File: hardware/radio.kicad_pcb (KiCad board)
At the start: 2 copper layers, 100 x 50 mm, 61 parts, among them J1 105450-0101, J2 Conn_01x02, J3 Conn_01x02, J4 Conn_01x04, J5 Conn_01x02_Male, Q1 Q_PMOS_DGS, Q2 Q_NMOS_DGS, Q3 Q_NMOS_DGS, Q4 Q_PMOS_DGS, SW1 SW_BOOT, SW2 SW_RST, SW3 SW_1, SW4 Rot_Enc, SW5 SW_2, SW6 SW_3, U1 TP4056, U2 ESP32-WROOM-32, U3 TPS5432, U4 MAX98357

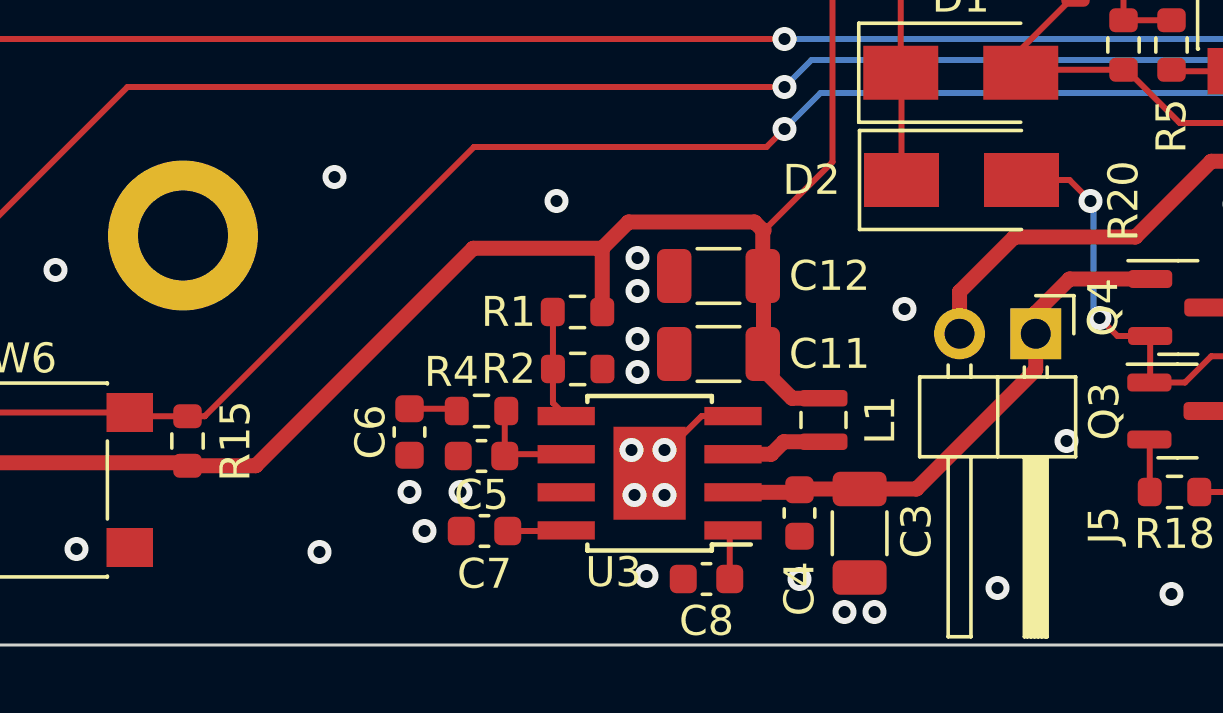
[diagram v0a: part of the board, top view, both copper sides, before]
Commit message: Fixed C8 connection from BOOT-GND to BOOT-PH
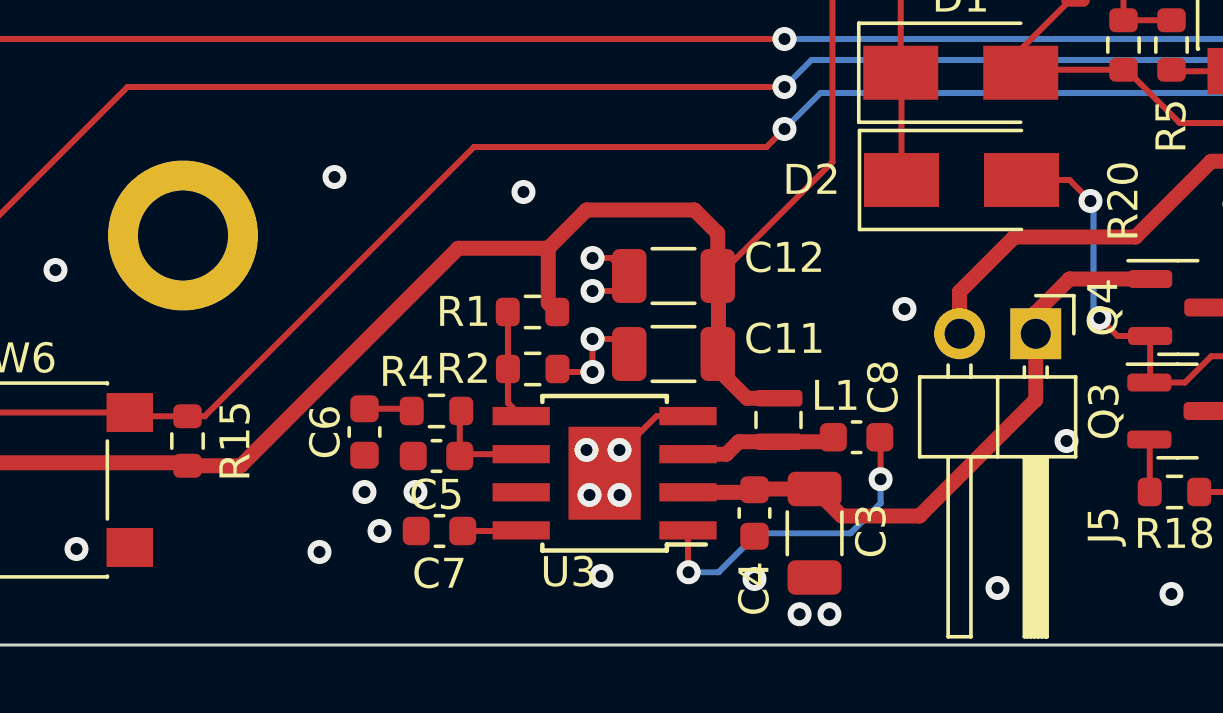
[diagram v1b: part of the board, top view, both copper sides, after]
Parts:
- moved C8 6.88 mm to (94.1, 73.1)
- moved C11 1.50 mm to (88.0, 70.3)
- moved C12 1.50 mm to (88.0, 67.7)
- moved C3 1.50 mm to (92.7, 76.3)
- moved C4 1.50 mm to (90.7, 75.6)
- moved C5 1.50 mm to (80.1, 73.7)
- moved C6 1.50 mm to (77.7, 72.9)
- moved C7 1.50 mm to (80.2, 76.2)
- moved L1 1.50 mm to (91.5, 72.5)
- moved R1 1.50 mm to (83.3, 68.9)
- moved R2 1.50 mm to (83.3, 70.8)
- moved R4 1.50 mm to (80.1, 72.2)
- moved U3 1.50 mm to (85.7, 74.3)
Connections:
- C8 pad 1: GND -> Net-(C8-Pad1)
- L1 pad 1: Net-(L1-Pad1) -> Net-(C8-Pad1)
- U3 pad 3: Net-(L1-Pad1) -> Net-(C8-Pad1)
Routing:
- net Net-(C8-Pad2): track 1.66 -> 11.0 mm, vias 0 -> 2
- net GND: track 55.6 -> 62.2 mm
- net Net-(C8-Pad1): track 0.00 -> 5.08 mm
- net Net-(L1-Pad1): track 3.19 -> 0.00 mm
- net Net-(C3-Pad1): track 18.0 -> 20.8 mm
- net +3V3: track 256.3 -> 257.3 mm

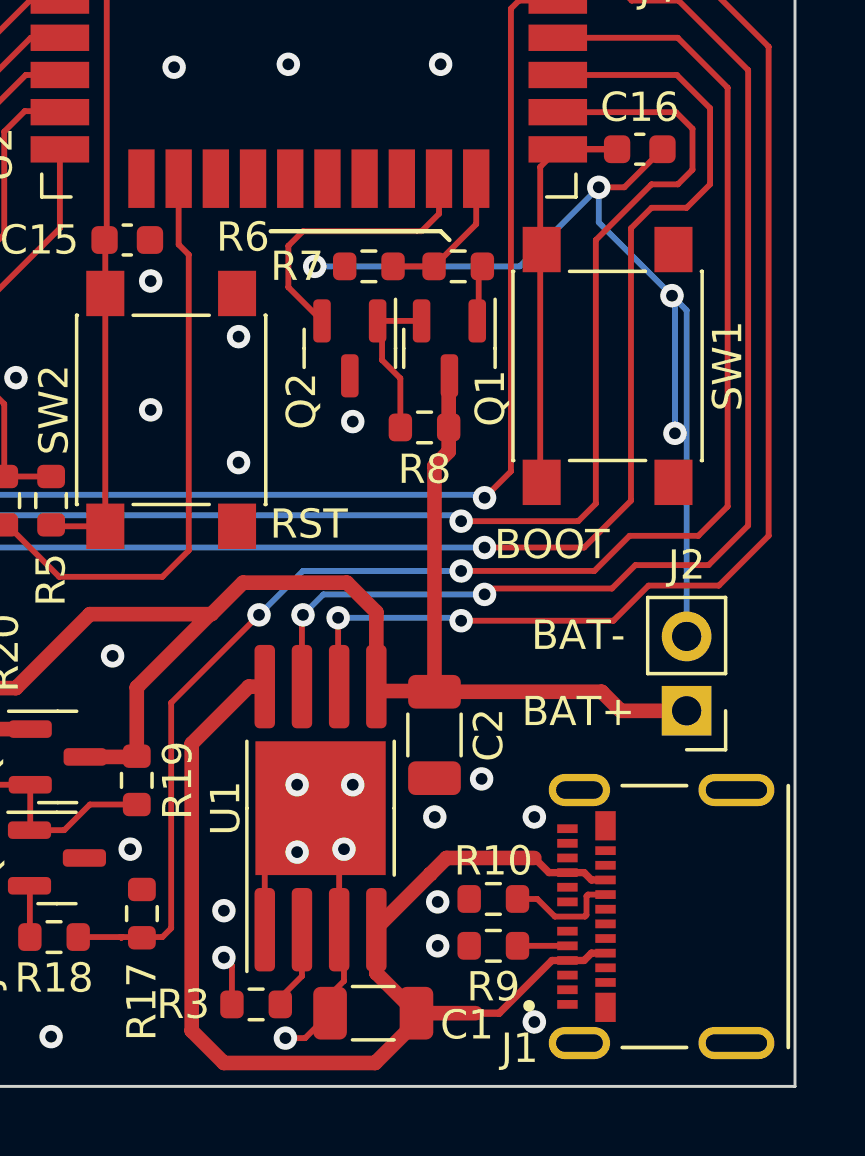
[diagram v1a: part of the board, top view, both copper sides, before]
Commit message: Added 0.4 ohm 0.5 W resistor to TP4056 to help with power dissipation
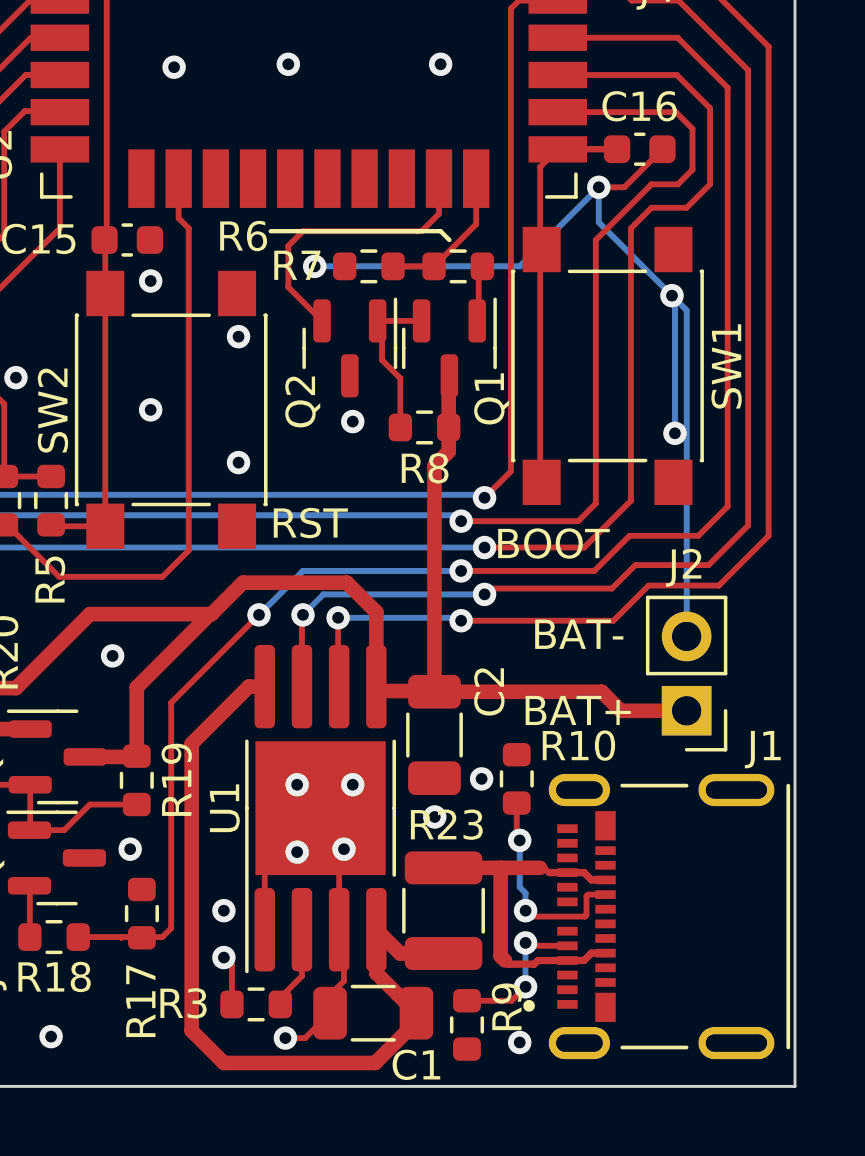
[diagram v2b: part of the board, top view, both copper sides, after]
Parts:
- added R23: 0.4, Resistor_SMD:R_1210_3225Metric, F.Cu at (118.0, 74.0)
- moved R10 4.18 mm to (120.5, 69.5), turned to 90 degrees
- moved R9 2.85 mm to (118.8, 77.9), turned to -90 degrees
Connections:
- C1 pad 1: +5V -> Net-(C1-Pad1)
- U1 pad 4: +5V -> Net-(C1-Pad1)
- U1 pad 8: +5V -> Net-(C1-Pad1)
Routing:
- net +5V: track 42.4 -> 13.0 mm
- net Net-(C1-Pad1): track 0.00 -> 28.2 mm
- net Net-(J1-PadA5): track 1.61 -> 5.17 mm, vias 0 -> 2
- net Net-(J1-PadB5): track 4.14 -> 7.50 mm, vias 0 -> 2
- net GND: vias 100 -> 97

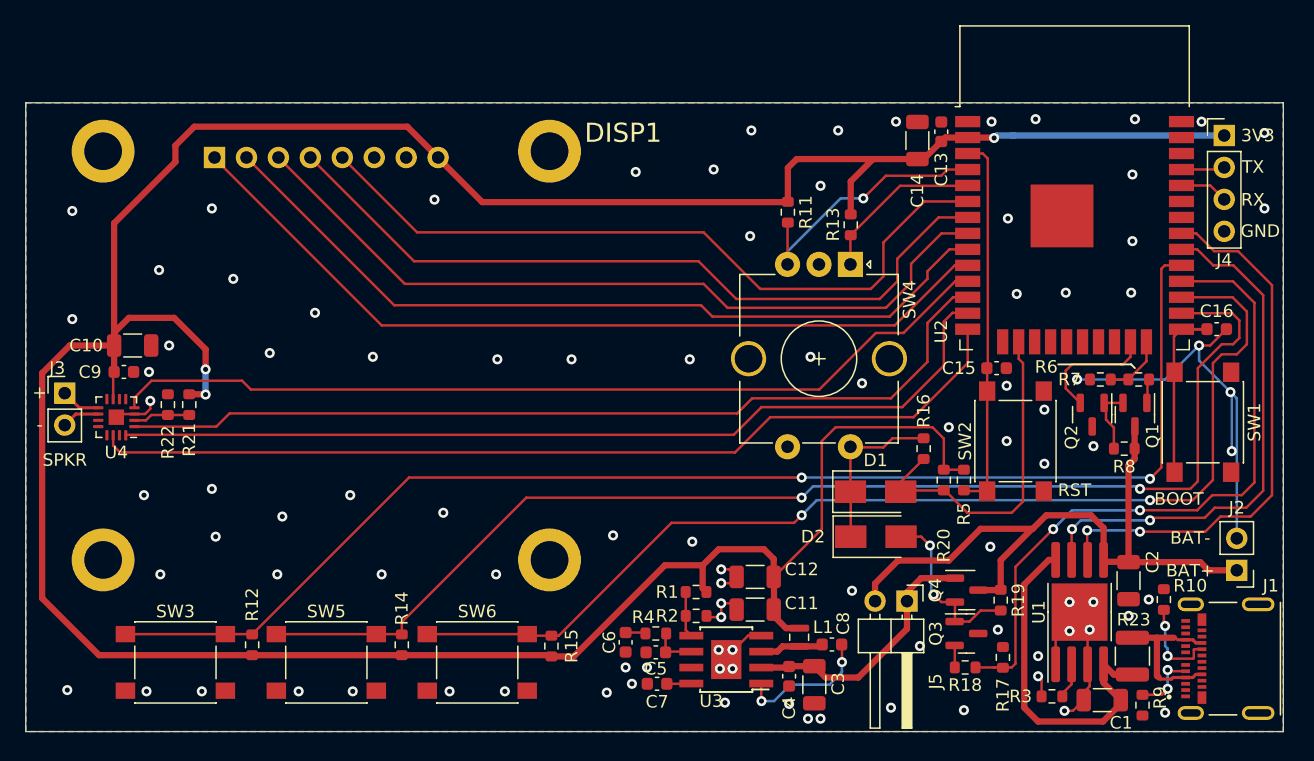
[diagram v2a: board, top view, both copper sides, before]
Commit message: adjusted silkscreen and some vias to improve labeling consistency and readability
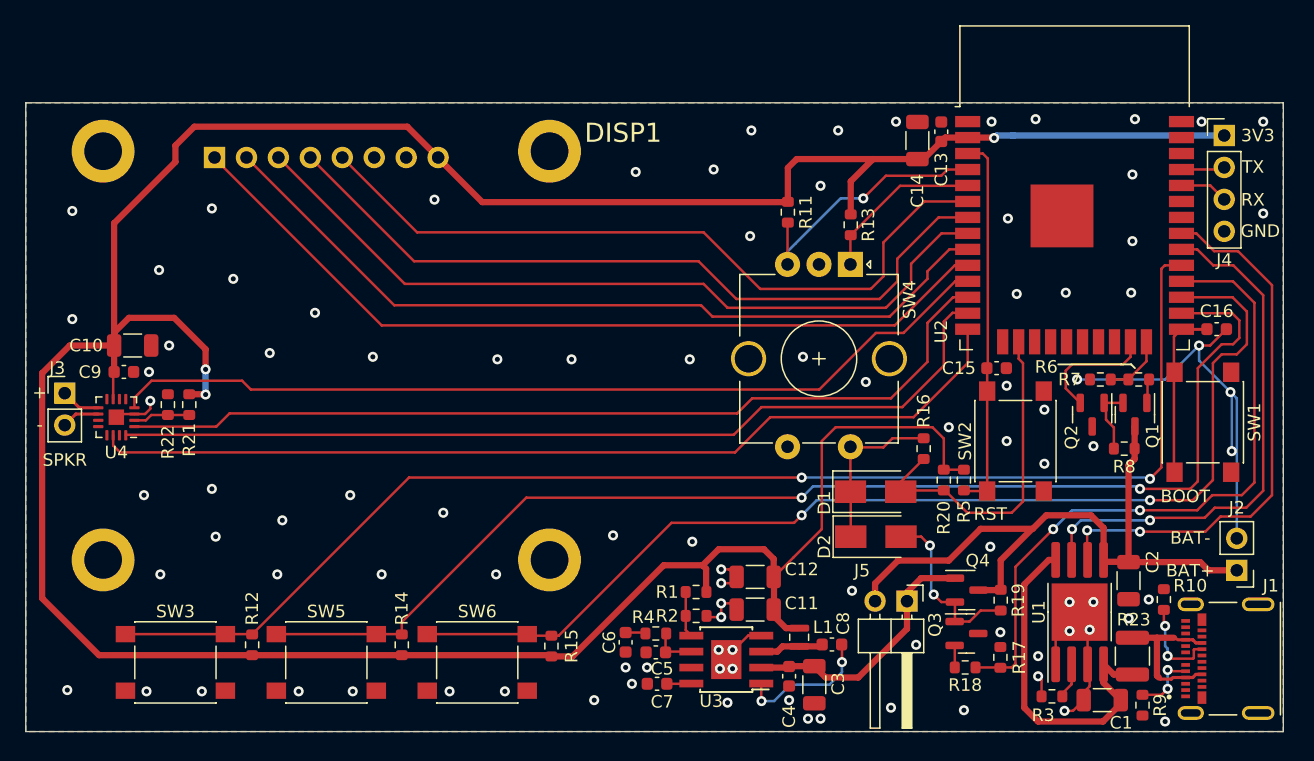
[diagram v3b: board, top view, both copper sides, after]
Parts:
- moved R17 0.20 mm to (107.5, 74.1)

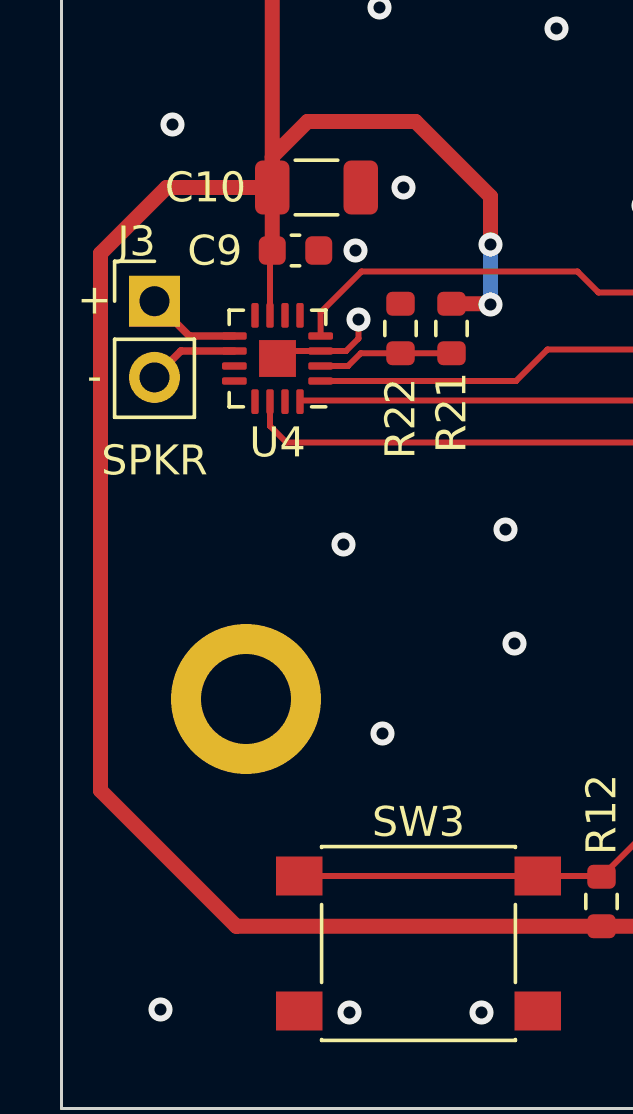
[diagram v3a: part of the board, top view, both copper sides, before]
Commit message: added copper fill cutout to the speaker connector and adjusted the 3V3 power trace near it to reduce potential proximity/ground-plane induced crosstalk
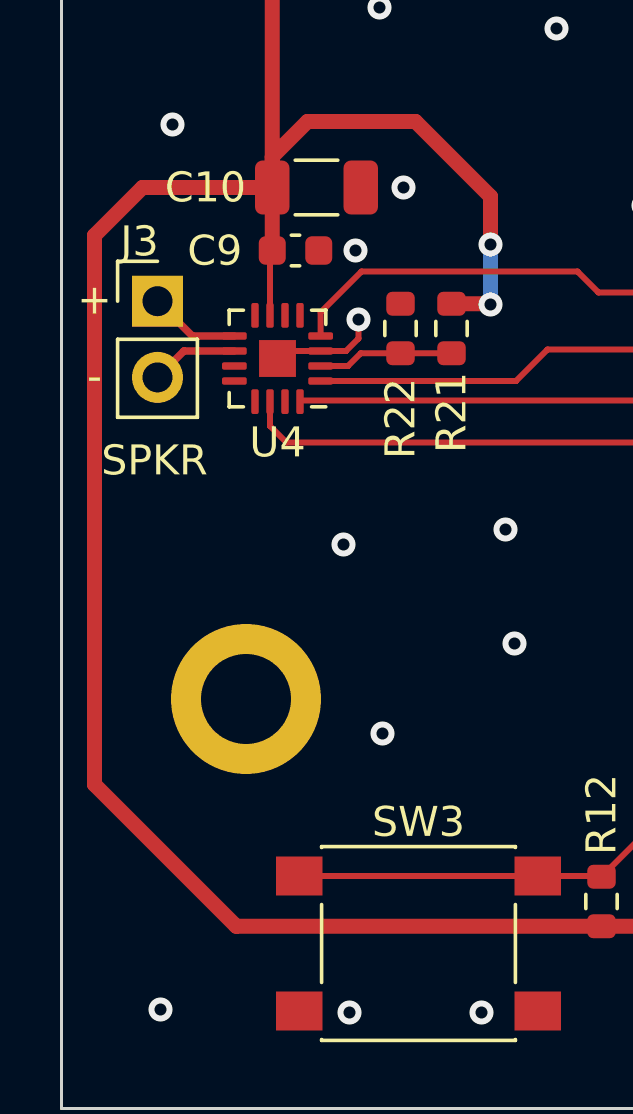
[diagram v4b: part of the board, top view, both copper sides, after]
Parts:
- moved J3 0.10 mm to (33.2, 53.1)
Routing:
- net +3V3: track 257.3 -> 257.9 mm
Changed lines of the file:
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@@
   )
   (footprint "Connector_PinHeader_2.54mm:PinHeader_1x02_P2.54mm_Vertical" (layer "F.Cu")
-    (at 33.1 53.09)
+    (at 33.2 53.09)
     (descr "Through hole straight pin header, 1x02, 2.54mm pitch, single row")
     (tags "Through hole pin header THT 1x02 2.54mm single row")
@@
   (segment (start 89.5 67.725) (end 89.475 67.7) (width 0.5) (layer "F.Cu") (net 7))
   (segment (start 94.4 55.8) (end 102.1 55.8) (width 0.2) (layer "F.Cu") (net 7))
+  (segment (start 31.1 69.2) (end 31.1 50.9) (width 0.5) (layer "F.Cu") (net 7))
   (segment (start 90.575 37.9) (end 90.6 37.875) (width 0.5) (layer "F.Cu") (net 7))
   (segment (start 89.5 67.7) (end 91.025 66.175) (width 0.2) (layer "F.Cu") (net 7))
@@
   (segment (start 102.1 55.8) (end 103 56.7) (width 0.2) (layer "F.Cu") (net 7))
   (segment (start 73.475 74.025) (end 80.725 66.775) (width 0.5) (layer "F.Cu") (net 7))
-  (segment (start 31.3 51.5) (end 33.5 49.3) (width 0.5) (layer "F.Cu") (net 7))
+  (segment (start 32.7 49.3) (end 37.025 49.3) (width 0.5) (layer "F.Cu") (net 7))
   (segment (start 43.4 31.9) (end 60.34 31.9) (width 0.5) (layer "F.Cu") (net 7))
   (segment (start 48 73.925) (end 59.9 73.925) (width 0.5) (layer "F.Cu") (net 7))
   (segment (start 95.6 36.25) (end 97.375 34.475) (width 0.5) (layer "F.Cu") (net 7))
+  (segment (start 31.1 50.9) (end 32.7 49.3) (width 0.5) (layer "F.Cu") (net 7))
   (segment (start 71.7 73.925) (end 71.8 74.025) (width 0.5) (layer "F.Cu") (net 7))
   (segment (start 43 53.175) (end 44.275 53.175) (width 0.5) (layer "F.Cu") (net 7))
   (segment (start 95.6 38.875) (end 95.6 36.25) (width 0.5) (layer "F.Cu") (net 7))
   (segment (start 60.34 31.9) (end 62.79 34.35) (width 0.5) (layer "F.Cu") (net 7))
-  (segment (start 48 73.925) (end 35.825 73.925) (width 0.5) (layer "F.Cu") (net 7))
   (segment (start 36.95 51.475) (end 37.025 51.4) (width 0.5) (layer "F.Cu") (net 7))
   (segment (start 103 59.175) (end 104.6 59.175) (width 0.2) (layer "F.Cu") (net 7))
@@
   (segment (start 71.8 74.025) (end 73.475 74.025) (width 0.5) (layer "F.Cu") (net 7))
   (segment (start 89.5 70.825) (end 89.5 67.725) (width 0.5) (layer "F.Cu") (net 7))
-  (segment (start 33.5 49.3) (end 37.025 49.3) (width 0.5) (layer "F.Cu") (net 7))
+  (segment (start 35.825 73.925) (end 31.1 69.2) (width 0.5) (layer "F.Cu") (net 7))
   (segment (start 85.1 65.5) (end 88.7 65.5) (width 0.5) (layer "F.Cu") (net 7))
   (segment (start 80.725 66.775) (end 83.825 66.775) (width 0.5) (layer "F.Cu") (net 7))
@@
   (segment (start 93.3 63.9) (end 93.3 56.9) (width 0.2) (layer "F.Cu") (net 7))
   (segment (start 104.9 32.765) (end 106.965 32.765) (width 0.5) (layer "F.Cu") (net 7))
-  (segment (start 31.3 69.4) (end 31.3 51.5) (width 0.5) (layer "F.Cu") (net 7))
+  (segment (start 48 73.925) (end 35.825 73.925) (width 0.5) (layer "F.Cu") (net 7))
   (segment (start 91.3 34.475) (end 97.375 34.475) (width 0.5) (layer "F.Cu") (net 7))
   (segment (start 41.8 47.1) (end 38.2 47.1) (width 0.5) (layer "F.Cu") (net 7))
   (segment (start 90.45 71.775) (end 89.5 70.825) (width 0.5) (layer "F.Cu") (net 7))
   (segment (start 103 56.7) (end 103 59.175) (width 0.2) (layer "F.Cu") (net 7))
-  (segment (start 35.825 73.925) (end 31.3 69.4) (width 0.5) (layer "F.Cu") (net 7))
   (segment (start 83.825 66.775) (end 84.1 67.05) (width 0.5) (layer "F.Cu") (net 7))
   (segment (start 102.8 33.075) (end 103.11 32.765) (width 0.5) (layer "F.Cu") (net 7))
@@
   (segment (start 103.7 46.7) (end 104.865 46.7) (width 0.2) (layer "F.Cu") (net 37))
   (segment (start 37.9875 56.4) (end 86.3 56.4) (width 0.2) (layer "F.Cu") (net 37))
-  (segment (start 34.26 54.25) (end 33.1 53.09) (width 0.25) (layer "F.Cu") (net 38))
-  (segment (start 35.7625 54.25) (end 34.26 54.25) (width 0.25) (layer "F.Cu") (net 38))
-  (segment (start 33.98 54.75) (end 33.1 55.63) (width 0.25) (layer "F.Cu") (net 39))
-  (segment (start 35.7625 54.75) (end 33.98 54.75) (width 0.25) (layer "F.Cu") (net 39))
+  (segment (start 34.36 54.25) (end 33.2 53.09) (width 0.25) (layer "F.Cu") (net 38))
+  (segment (start 35.7625 54.25) (end 34.36 54.25) (width 0.25) (layer "F.Cu") (net 38))
+  (segment (start 34.08 54.75) (end 33.2 55.63) (width 0.25) (layer "F.Cu") (net 39))
+  (segment (start 35.7625 54.75) (end 34.08 54.75) (width 0.25) (layer "F.Cu") (net 39))
   (segment (start 77.7 72.125) (end 79.1 72.125) (width 0.2) (layer "F.Cu") (net 40))
   (segment (start 79.1 72.125) (end 79.175 72.2) (width 0.2) (layer "F.Cu") (net 40))
@@
       )
     )
+  )
+  (zone (net 0) (net_name "") (layers F&B.Cu) (hatch edge 0.508)
+    (connect_pads (clearance 0))
+    (min_thickness 0.254)
+    (keepout (tracks allowed) (vias allowed) (pads allowed) (copperpour not_allowed) (footprints allowed))
+    (fill (thermal_gap 0.508) (thermal_bridge_width 0.508))
+    (polygon
+      (pts
+        (xy 35.1 57.4)
+        (xy 31.7 57.4)
+        (xy 31.7 51.3)
+        (xy 35.1 51.3)
+      )
+    )
